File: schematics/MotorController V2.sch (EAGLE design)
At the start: 53 parts, among them IC1 7805, Q1 BC307

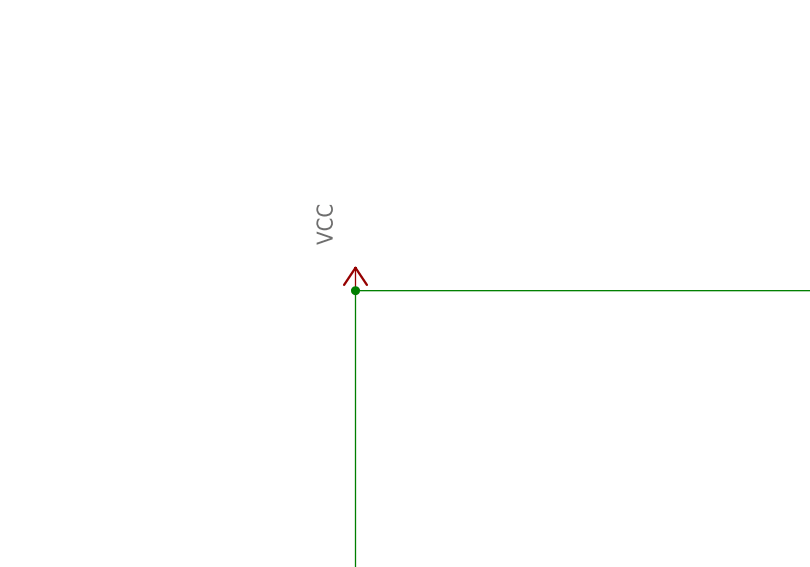
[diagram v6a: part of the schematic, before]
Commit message: board now with ESP8266
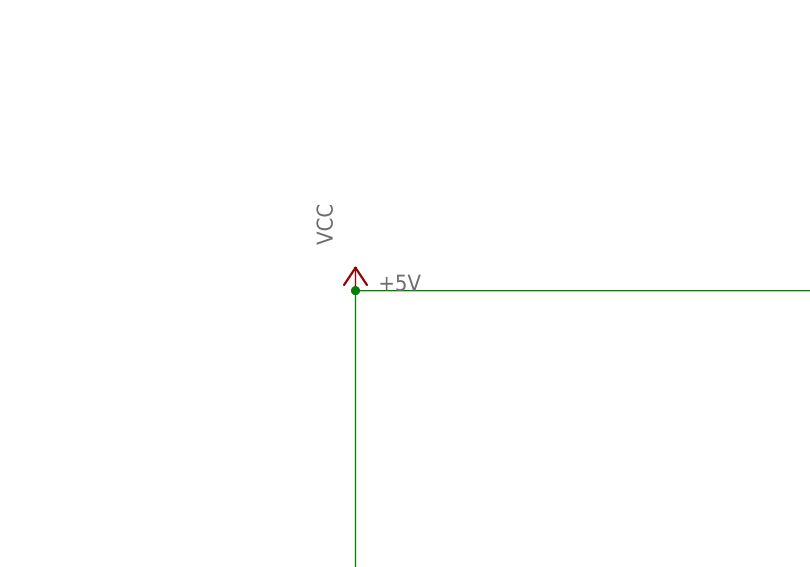
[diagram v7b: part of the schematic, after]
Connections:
- net CTRL-5.0V renamed +5V
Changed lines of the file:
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@@
 </busses>
 <nets>
-<net name="CTRL-5.0V" class="0">
+<net name="+5V" class="0">
 <segment>
 <pinref part="P+1" gate="VCC" pin="VCC"/>
@@
 <pinref part="CONTROL" gate="1" pin="3"/>
 <wire x1="134.62" y1="167.64" x2="154.94" y2="167.64" width="0.1524" layer="91"/>
+<label x="-68.58" y="149.86" size="1.778" layer="95"/>
 </segment>
 </net>

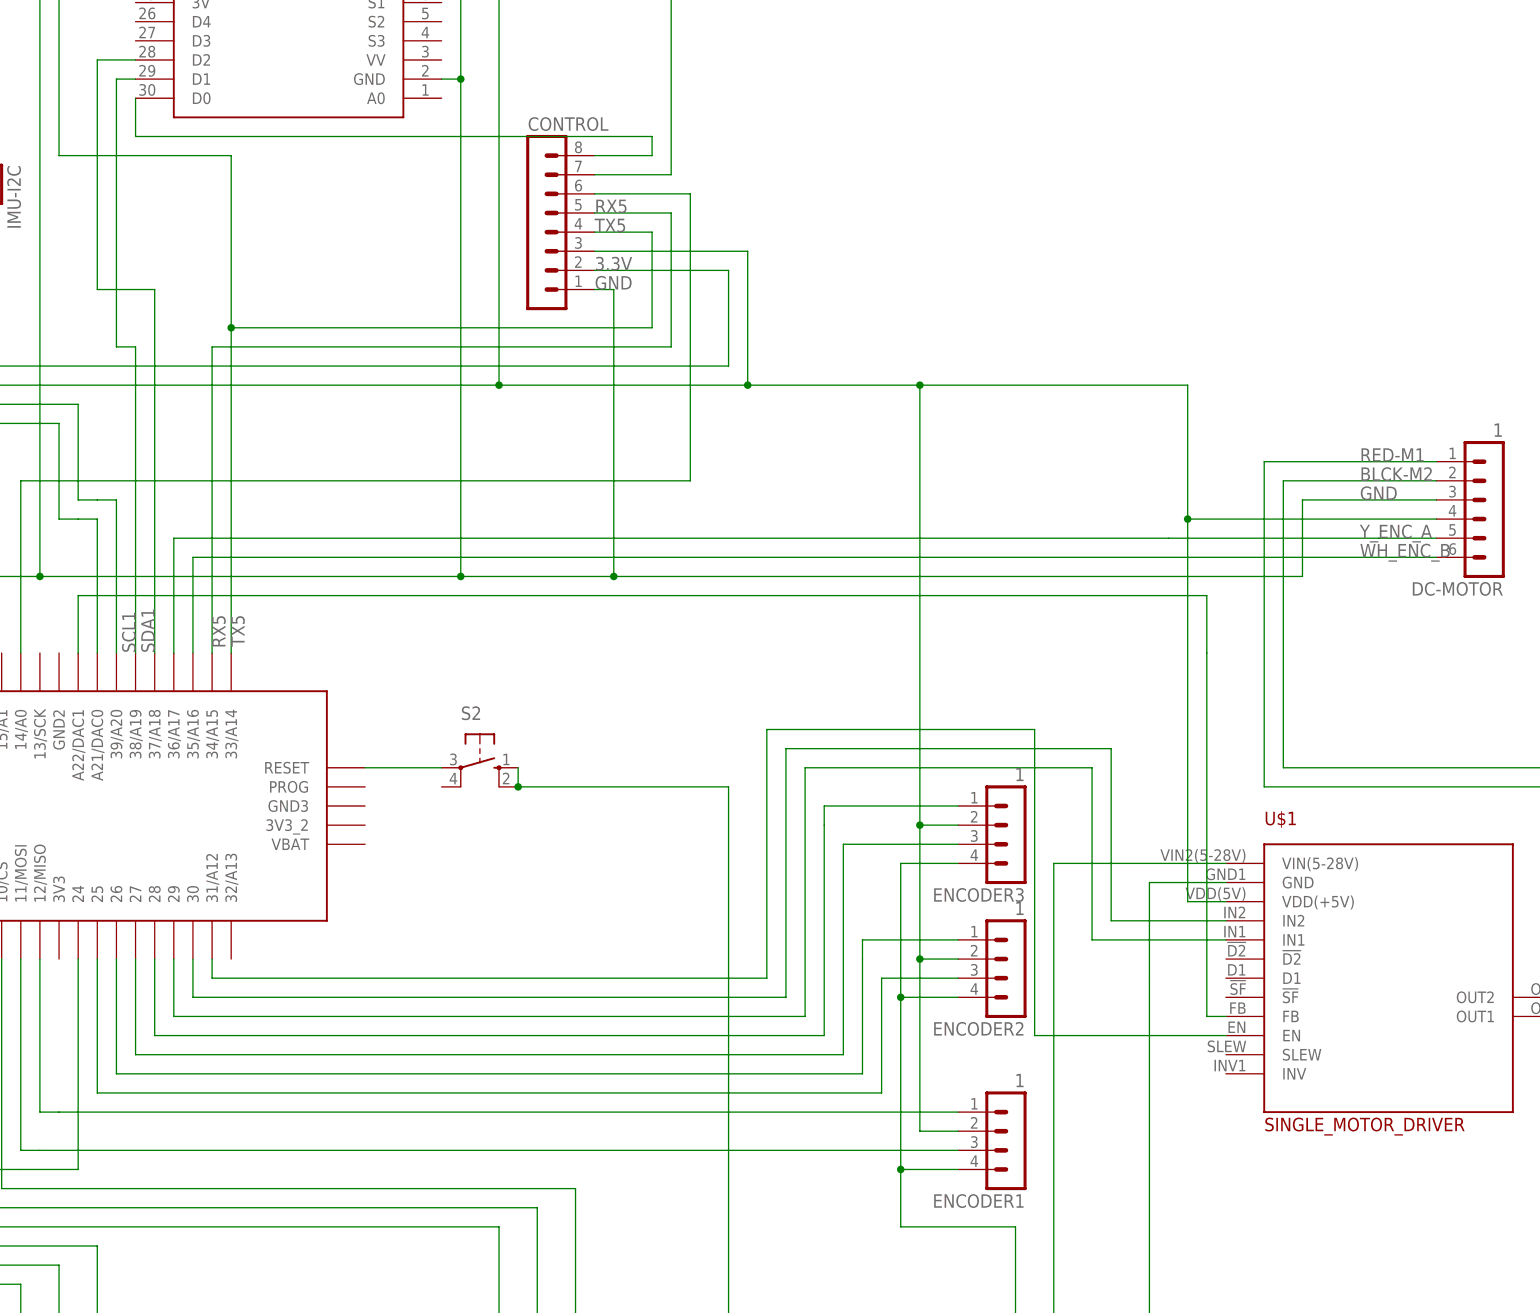
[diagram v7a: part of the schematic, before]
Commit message: new class I2CMaster
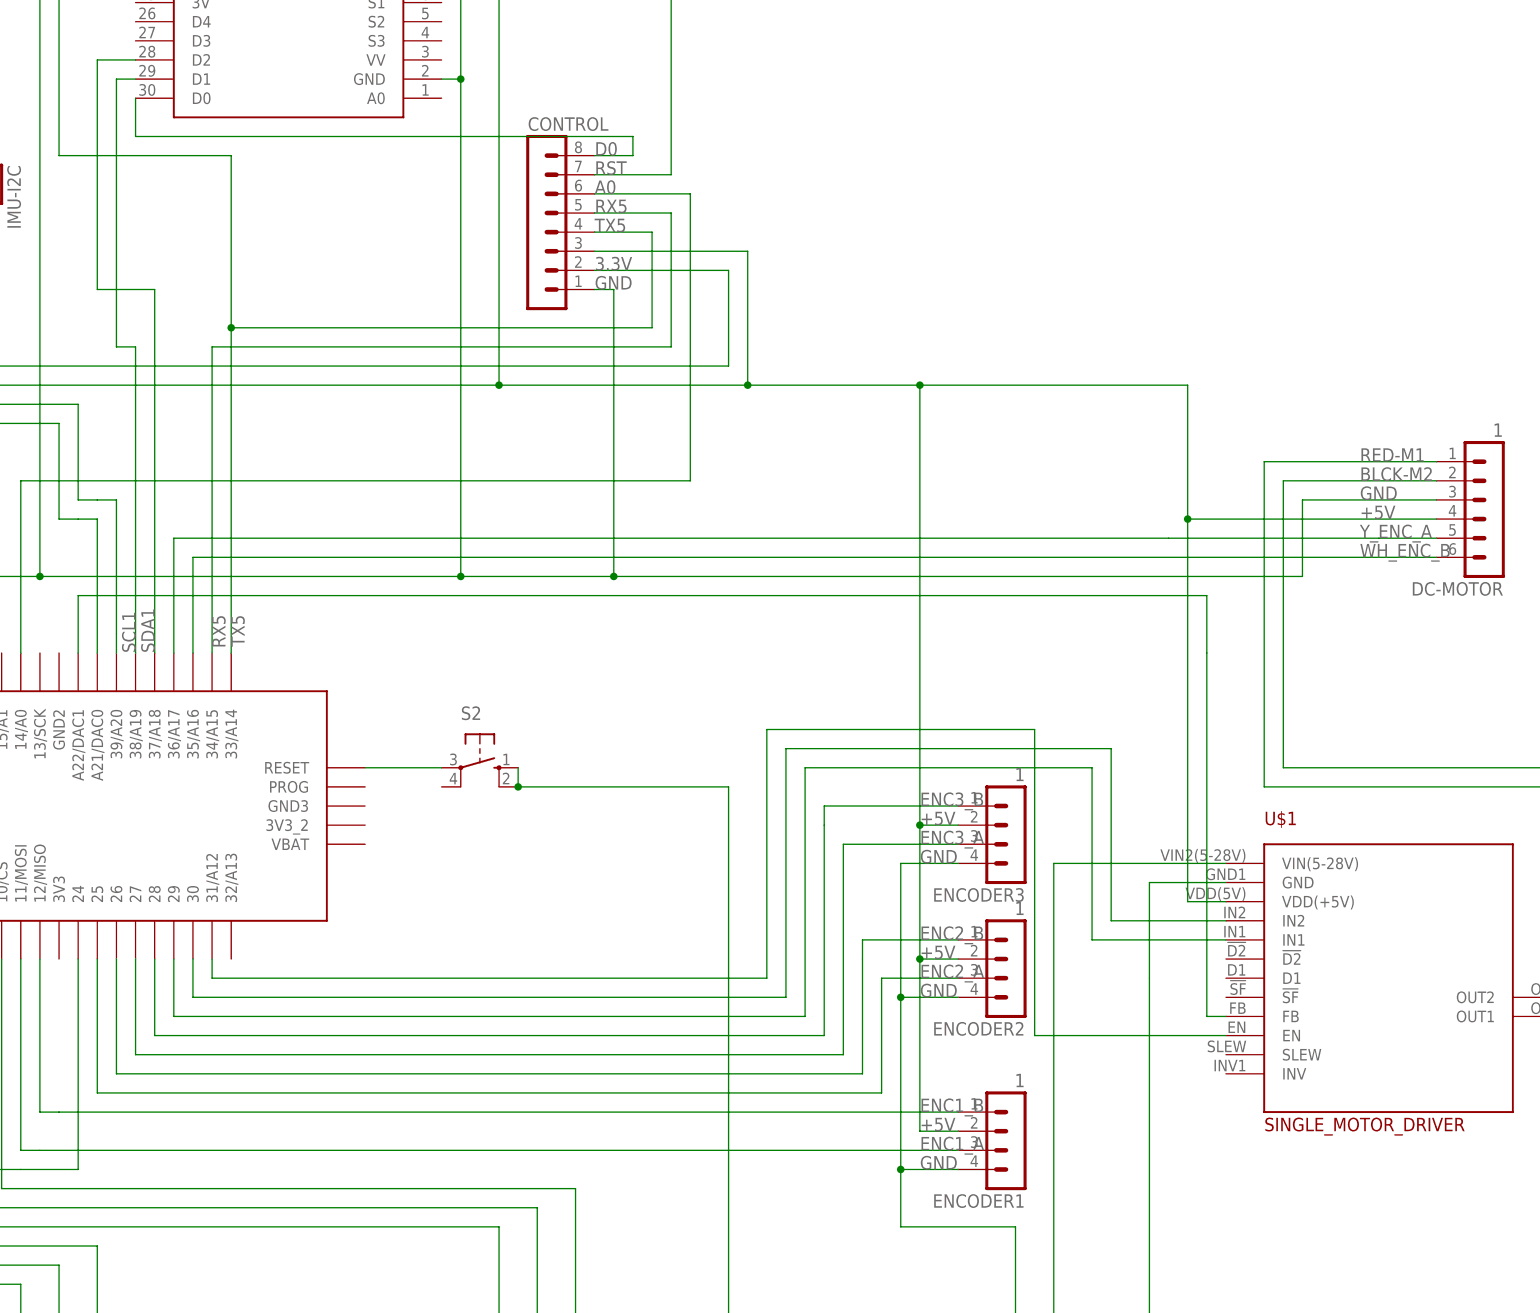
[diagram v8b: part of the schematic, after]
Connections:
- net N$33 renamed ENC1_A
- net N$34 renamed ENC1_B
- net N$35 renamed ENC2_A
- net N$36 renamed ENC2_B
- net N$37 renamed ENC3_A
- net N$38 renamed ENC3_B
- net N$49 renamed D0
- net N$50 renamed RST
- net N$51 renamed A0
